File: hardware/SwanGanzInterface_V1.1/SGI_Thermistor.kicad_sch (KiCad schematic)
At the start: 20 parts, among them J3 Conn_01x03_Pin, U8 INA122D, U9 OPA2350

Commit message: Added lots, moving to 64 pin micro
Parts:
- R15: value 8k2 -> 27k
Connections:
- net +3V3: no longer R14.1, R16.1
- new net Therm_Voltage+: R14.1, R16.1
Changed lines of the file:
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@@
-	(wire
-		(pts
-			(xy 44.45 45.212) (xy 44.45 47.244)
-		)
-		(stroke
-			(width 0)
-			(type default)
-		)
-	)
 	(wire
 		(pts
@@
 	(wire
 		(pts
+			(xy 44.45 45.466) (xy 44.45 47.244)
+		)
+		(stroke
+			(width 0)
+			(type default)
+		)
+	)
+	(wire
+		(pts
 			(xy 101.6 40.64) (xy 101.6 35.56)
 		)
@@
 	(wire
 		(pts
+			(xy 66.294 29.464) (xy 66.294 32.004)
+		)
+		(stroke
+			(width 0)
+			(type default)
+		)
+	)
+	(wire
+		(pts
 			(xy 200.66 53.34) (xy 204.47 53.34)
 		)
@@
 	(wire
 		(pts
+			(xy 59.69 29.464) (xy 66.294 29.464)
+		)
+		(stroke
+			(width 0)
+			(type default)
+		)
+	)
+	(wire
+		(pts
 			(xy 265.43 26.67) (xy 265.43 25.4)
 		)
@@
 	(wire
 		(pts
+			(xy 41.656 45.466) (xy 44.45 45.466)
+		)
+		(stroke
+			(width 0)
+			(type default)
+		)
+	)
+	(wire
+		(pts
 			(xy 189.23 83.82) (xy 184.15 83.82)
 		)
@@
 		(pts
 			(xy 134.62 64.77) (xy 134.62 62.23)
-		)
-		(stroke
-			(width 0)
-			(type default)
-		)
-	)
-	(wire
-		(pts
-			(xy 66.294 29.972) (xy 66.294 32.004)
 		)
 		(stroke
@@
 		)
 	)
+	(global_label "Therm_Voltage+"
+		(shape input)
+		(at 59.69 29.464 180)
+		(fields_autoplaced yes)
+		(effects
+			(font
+				(size 1.27 1.27)
+			)
+			(justify right)
+		)
+		(property "Intersheetrefs" "${INTERSHEET_REFS}"
+			(at 41.465 29.464 0)
+			(effects
+				(font
+					(size 1.27 1.27)
+				)
+				(justify right)
+				(hide yes)
+			)
+		)
+	)
 	(global_label "THERM_LG_A0.0"
 		(shape input)
@@
 				)
 				(justify left)
+				(hide yes)
+			)
+		)
+	)
+	(global_label "Therm_Voltage+"
+		(shape input)
+		(at 41.656 45.466 180)
+		(fields_autoplaced yes)
+		(effects
+			(font
+				(size 1.27 1.27)
+			)
+			(justify right)
+		)
+		(property "Intersheetrefs" "${INTERSHEET_REFS}"
+			(at 23.431 45.466 0)
+			(effects
+				(font
+					(size 1.27 1.27)
+				)
+				(justify right)
 				(hide yes)
 			)
@@
 	)
 	(symbol
-		(lib_id "power:+3V3")
-		(at 44.45 45.212 0)
-		(unit 1)
-		(exclude_from_sim no)
-		(in_bom yes)
-		(on_board yes)
-		(dnp no)
-		(fields_autoplaced yes)
-		(property "Reference" "#PWR035"
-			(at 44.45 49.022 0)
-			(effects
-				(font
-					(size 1.27 1.27)
-				)
-				(hide yes)
-			)
-		)
-		(property "Value" "+3V3"
-			(at 44.45 40.894 0)
-			(effects
-				(font
-					(size 1.27 1.27)
-				)
-			)
-		)
-		(property "Footprint" ""
-			(at 44.45 45.212 0)
-			(effects
-				(font
-					(size 1.27 1.27)
-				)
-				(hide yes)
-			)
-		)
-		(property "Datasheet" ""
-			(at 44.45 45.212 0)
-			(effects
-				(font
-					(size 1.27 1.27)
-				)
-				(hide yes)
-			)
-		)
-		(property "Description" "Power symbol creates a global label with name \"+3V3\""
-			(at 44.45 45.212 0)
-			(effects
-				(font
-					(size 1.27 1.27)
-				)
-				(hide yes)
-			)
-		)
-		(pin "1"
-		)
-		(instances
-			(project "SwanGanzInterface"
-				(path "/4e9a6e30-f660-472b-9696-bea1f34b4545/2d5e901e-83ed-4d76-b163-6429564a2d4c"
-					(reference "#PWR035")
-					(unit 1)
-				)
-			)
-		)
-	)
-	(symbol
 		(lib_id "Device:R")
 		(at 66.294 35.814 0)
@@
 			)
 		)
-		(property "Value" "8k2"
+		(property "Value" "27k"
 			(at 44.45 66.04 90)
 			(effects
@@
 					(unit 1)
 				)
-			)
-		)
-	)
-	(symbol
-		(lib_id "power:+3V3")
-		(at 66.294 29.972 0)
-		(unit 1)
-		(exclude_from_sim no)
-		(in_bom yes)
-		(on_board yes)
-		(dnp no)
-		(fields_autoplaced yes)
-		(property "Reference" "#PWR038"
-			(at 66.294 33.782 0)
-			(effects
-				(font
-					(size 1.27 1.27)
-				)
-				(hide yes)
-			)
-		)
-		(property "Value" "+3V3"
-			(at 66.294 25.654 0)
-			(effects
-				(font
-					(size 1.27 1.27)
-				)
-			)
-		)
-		(property "Footprint" ""
-			(at 66.294 29.972 0)
-			(effects
-				(font
-					(size 1.27 1.27)
-				)
-				(hide yes)
-			)
-		)
-		(property "Datasheet" ""
-			(at 66.294 29.972 0)
-			(effects
-				(font
-					(size 1.27 1.27)
-				)
-				(hide yes)
-			)
-		)
-		(property "Description" "Power symbol creates a global label with name \"+3V3\""
-			(at 66.294 29.972 0)
-			(effects
-				(font
-					(size 1.27 1.27)
-				)
-				(hide yes)
-			)
-		)
-		(pin "1"
-		)
-		(instances
-			(project ""
-				(path "/4e9a6e30-f660-472b-9696-bea1f34b4545/2d5e901e-83ed-4d76-b163-6429564a2d4c"
-					(reference "#PWR038")
-					(unit 1)
-				)

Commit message: Schematic Check
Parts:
- R15: renamed from R17; value 65k5 -> 27k
- R18: renamed from R20; now not fitted
- R21: renamed from R23; value 10k -> 8.2k
- renumbered C10 to C15, C11 to C16, C12 to C17, C13 to C18, R14 to R12, R15 to R13, R16 to R14, R18 to R16, R19 to R17, R21 to R19, R22 to R20, TP9 to TP8, TP8 to TP9, U8 to U5, U9 to U6
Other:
- note added: "Gain : G = 1 + (Rf / Rg) G = 1 + (0 / 10k) = 1"
- note added: "Gain : G = 1 + (Rf / Rg) G = 1 + (8.2k / 10k) = 1.82"
- note added: "Gain : G = 5 + (200k / Rg) G = 5 + (200k / 27k) = 12.407"
- note added: "Total Gain : 12.407 * 1 * 1.82 = 22.581"
- note added: "Total Gain : 12.407 * 1 = 12.407"
- note removed: "Gain : G = 1 + (Rf / Rg) G = 1 + (10k / 10k) = 2"
- note removed: "Gain : G = 5 + (200k / Rg) G = 5 + (200k / 65k5) = 3.053"
- note removed: "Total Gain : 3.053 * 2 * 2 = 12.214"
- note removed: "Total Gain : 3.053 * 2 = 6.107"
- moved on the sheet: TP8, TP9

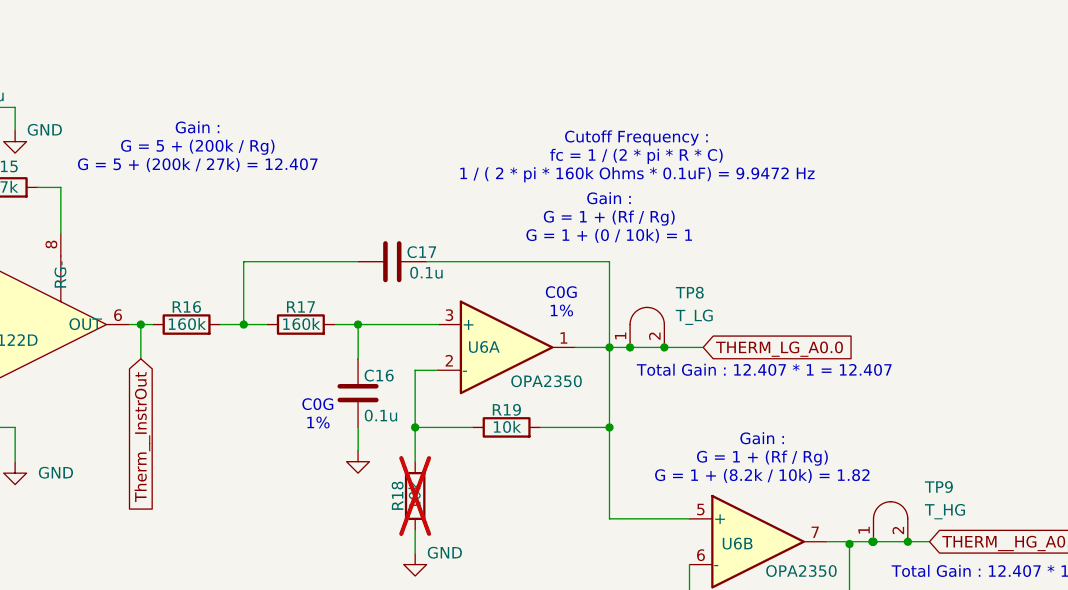
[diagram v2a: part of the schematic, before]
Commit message: Filter paramaters and assigned footprints
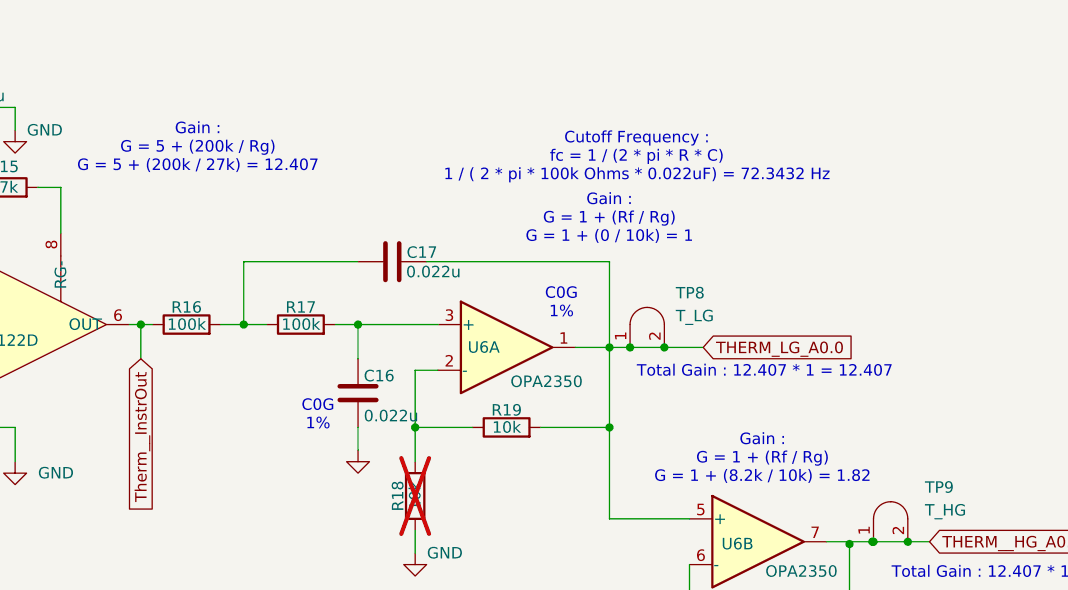
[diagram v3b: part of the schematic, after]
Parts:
- C16, C17: value 0.1u -> 0.022u; footprint Capacitor_SMD:C_1206_3216Metric -> Capacitor_SMD:C_0805_2012Metric
- R16, R17: value 160k -> 100k
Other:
- note added: "Cutoff Frequency : fc = 1 / (2 * pi * R * C) 1 / ( 2 * pi * 100k Ohms * 0.022uF) = 72.3432 Hz"
- note removed: "Cutoff Frequency : fc = 1 / (2 * pi * R * C) 1 / ( 2 * pi * 160k Ohms * 0.1uF) = 9.9472 Hz"
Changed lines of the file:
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@@
 		)
 	)
-	(text "Cutoff Frequency :\nfc = 1 / (2 * pi * R * C)\n1 / ( 2 * pi * 160k Ohms * 0.1uF) = 9.9472 Hz"
+	(text "Cutoff Frequency :\nfc = 1 / (2 * pi * R * C)\n1 / ( 2 * pi * 100k Ohms * 0.022uF) = 72.3432 Hz"
 		(exclude_from_sim no)
 		(at 165.608 32.258 0)
@@
 			)
 		)
-		(property "Value" "160k"
+		(property "Value" "100k"
 			(at 115.57 50.8 90)
 			(effects
@@
 			)
 		)
-		(property "Value" "160k"
+		(property "Value" "100k"
 			(at 128.27 50.8 90)
 			(effects
@@
 			)
 		)
-		(property "Value" "0.1u"
+		(property "Value" "0.022u"
 			(at 135.255 60.96 0)
 			(effects
@@
 			)
 		)
-		(property "Footprint" "Capacitor_SMD:C_1206_3216Metric"
+		(property "Footprint" "Capacitor_SMD:C_0805_2012Metric"
 			(at 135.5852 62.23 0)
 			(effects
@@
 			)
 		)
-		(property "Value" "0.1u"
-			(at 142.24 45.085 90)
-			(effects
-				(font
-					(size 1.27 1.27)
-				)
-			)
-		)
-		(property "Footprint" "Capacitor_SMD:C_1206_3216Metric"
+		(property "Value" "0.022u"
+			(at 143.002 44.958 90)
+			(effects
+				(font
+					(size 1.27 1.27)
+				)
+			)
+		)
+		(property "Footprint" "Capacitor_SMD:C_0805_2012Metric"
 			(at 142.24 42.8498 0)
 			(effects
